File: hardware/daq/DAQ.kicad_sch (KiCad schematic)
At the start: 186 parts, among them J1 ICD15S13E4GX00LF, J2 ICD15S13E4GX00LF, J3 ICD15S13E4GX00LF, J4 ICD15S13E4GX00LF, P1 0022272021, U1 ADS124S08IRHBT, U11 SN74AHCT125RGYR, U2 ADS124S08IRHBT, U3 LT6654BMPS6-5-TRMPBF, U4 LM1086IS-5.0_NOPB, U5 TPS73801DCQR, U6 TPSM63603RDHR, U7 TPSM63603RDHR, U8 TPSM63603RDHR, U9 ADS124S08IRHBT

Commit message: routed 1.75 DSUBs
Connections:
- net FMV: now also D10.4; no longer D9.4
- net IDAC2_2: now also J1.12; no longer J1.11
- net PT10_SIG: now also J3.6; no longer J3.4
- net PT11_SIG: now also D3.4, J3.4; no longer D3.6, J3.6
- net PT12_SIG: now also D3.6, J3.14; no longer D3.4, J3.11
- net PT3_SIG: now also D9.4, J3.11; no longer D2.1, J3.14
- net PT7_SIG: now also D2.6; no longer D1.6
- net PT9_SIG: now also D1.6; no longer D2.6
- net RTD1_L1: now also J1.1; no longer J1.2
- net RTD1_L3: now also J1.2; no longer J1.1
- net RTD2_L1: now also J1.14; no longer J1.13
- net RTD2_L3: now also J1.13; no longer J1.12
- net RTD3_L3: now also J1.11; no longer J1.14

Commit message: 2 DSUBs???
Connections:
- net IDAC2_1: now also J2.14; no longer J1.3
- net PT4_SIG: now also J1.1; no longer J2.12
- net PT5_SIG: now also J1.2; no longer J2.13
- net PT6_SIG: now also J1.3; no longer J2.14
- net RTD1_L1: now also J2.12; no longer J1.1
- net RTD1_L3: now also J2.13; no longer J1.2
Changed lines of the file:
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@@
-		)
-	)
-	(label "PT4_SIG"
-		(at 347.98 346.71 0)
-		(fields_autoplaced yes)
-		(effects
-			(font
-				(size 1.27 1.27)
-			)
-			(justify left bottom)
-		)
-		(property "Netclass" ""
-			(at 347.98 347.98 0)
-			(effects
-				(font
-					(size 1.27 1.27)
-					(italic yes)
-				)
-				(justify left)
-			)
-		)
-	)
-	(label "PT6_SIG"
-		(at 347.98 351.79 0)
-		(fields_autoplaced yes)
-		(effects
-			(font
-				(size 1.27 1.27)
-			)
-			(justify left bottom)
-		)
-		(property "Netclass" ""
-			(at 347.98 353.06 0)
-			(effects
-				(font
-					(size 1.27 1.27)
-					(italic yes)
-				)
-				(justify left)
-			)
 		)
 	)
@@
 		)
 	)
+	(label "PT4_SIG"
+		(at 257.81 344.17 0)
+		(fields_autoplaced yes)
+		(effects
+			(font
+				(size 1.27 1.27)
+			)
+			(justify left bottom)
+		)
+		(property "Netclass" ""
+			(at 257.81 345.44 0)
+			(effects
+				(font
+					(size 1.27 1.27)
+					(italic yes)
+				)
+				(justify left)
+			)
+		)
+	)
 	(label "PT11_SIG"
 		(at 364.49 351.79 0)
@@
 		)
 	)
+	(label "PT5_SIG"
+		(at 257.81 346.71 0)
+		(fields_autoplaced yes)
+		(effects
+			(font
+				(size 1.27 1.27)
+			)
+			(justify left bottom)
+		)
+		(property "Netclass" ""
+			(at 257.81 347.98 0)
+			(effects
+				(font
+					(size 1.27 1.27)
+					(italic yes)
+				)
+				(justify left)
+			)
+		)
+	)
 	(label "LS1_SIG-"
 		(at 41.91 95.25 0)
@@
 		)
 	)
-	(label "RTD1_L1"
-		(at 257.81 344.17 0)
-		(effects
-			(font
-				(size 1.27 1.27)
-			)
-			(justify left bottom)
-		)
-	)
 	(label "IDAC2_1"
 		(at 53.34 76.2 0)
@@
 		)
 	)
+	(label "RTD1_L1"
+		(at 347.98 346.71 0)
+		(effects
+			(font
+				(size 1.27 1.27)
+			)
+			(justify left bottom)
+		)
+	)
 	(label "SCLK"
 		(at 218.44 91.44 0)
@@
 		)
 	)
+	(label "RTD1_L2"
+		(at 347.98 351.79 0)
+		(effects
+			(font
+				(size 1.27 1.27)
+			)
+			(justify left bottom)
+		)
+	)
 	(label "DATA_BUS"
 		(at 273.05 200.66 0)
@@
 		)
 	)
-	(label "PT5_SIG"
-		(at 347.98 349.25 0)
-		(fields_autoplaced yes)
-		(effects
-			(font
-				(size 1.27 1.27)
-			)
-			(justify left bottom)
-		)
-		(property "Netclass" ""
-			(at 347.98 350.52 0)
-			(effects
-				(font
-					(size 1.27 1.27)
-					(italic yes)
-				)
-				(justify left)
-			)
-		)
-	)
 	(label "FMV"
 		(at 443.23 54.61 0)
@@
 		)
 	)
+	(label "PT6_SIG"
+		(at 257.81 349.25 0)
+		(fields_autoplaced yes)
+		(effects
+			(font
+				(size 1.27 1.27)
+			)
+			(justify left bottom)
+		)
+		(property "Netclass" ""
+			(at 257.81 350.52 0)
+			(effects
+				(font
+					(size 1.27 1.27)
+					(italic yes)
+				)
+				(justify left)
+			)
+		)
+	)
 	(label "IDAC2_1"
 		(at 147.32 78.74 0)
@@
 		)
 	)
+	(label "RTD1_L3"
+		(at 347.98 349.25 0)
+		(effects
+			(font
+				(size 1.27 1.27)
+			)
+			(justify left bottom)
+		)
+	)
 	(label "LS2_SIG-"
 		(at 312.42 351.79 0)
@@
 		)
 	)
-	(label "RTD1_L3"
-		(at 257.81 346.71 0)
-		(effects
-			(font
-				(size 1.27 1.27)
-			)
-			(justify left bottom)
-		)
-	)
 	(label "OIMV{slash}FIMV{slash}SPARK"
 		(at 537.21 64.77 0)
@@
 		(effects
 			(font
-				(size 1.27 1.27)
-			)
-			(justify left bottom)
-		)
-	)
-	(label "RTD1_L2"
-		(at 257.81 349.25 0)
-		(effects
-			(font

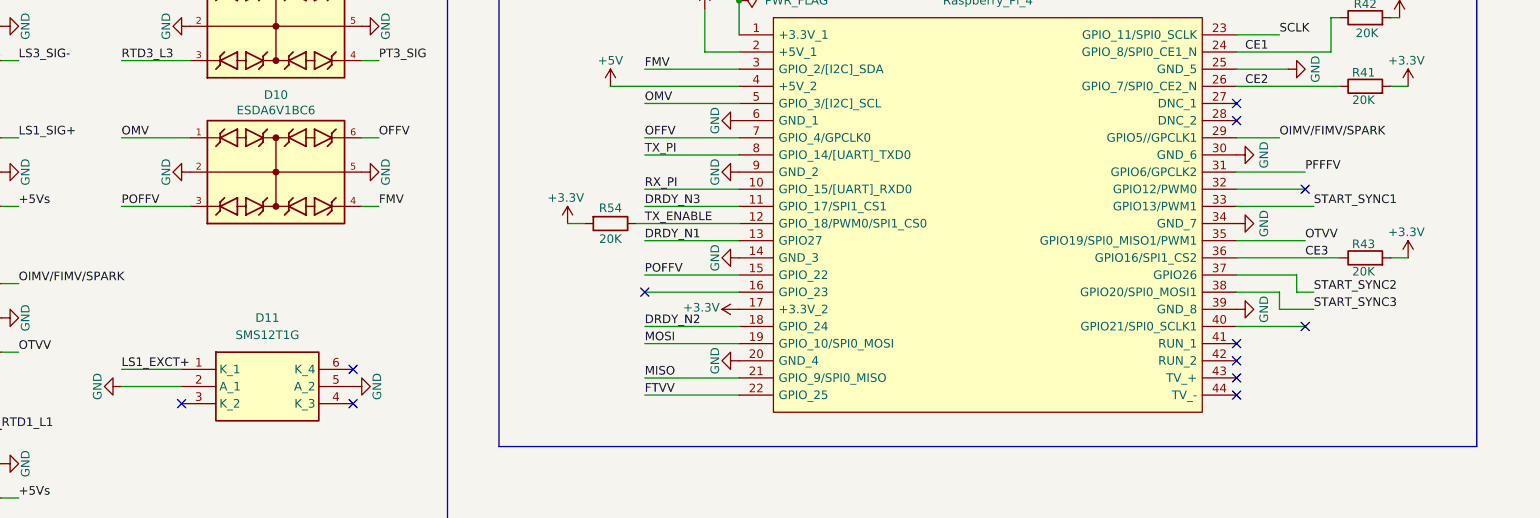
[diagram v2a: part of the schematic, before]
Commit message: routed valve actuation traces thu TVS and GPIO
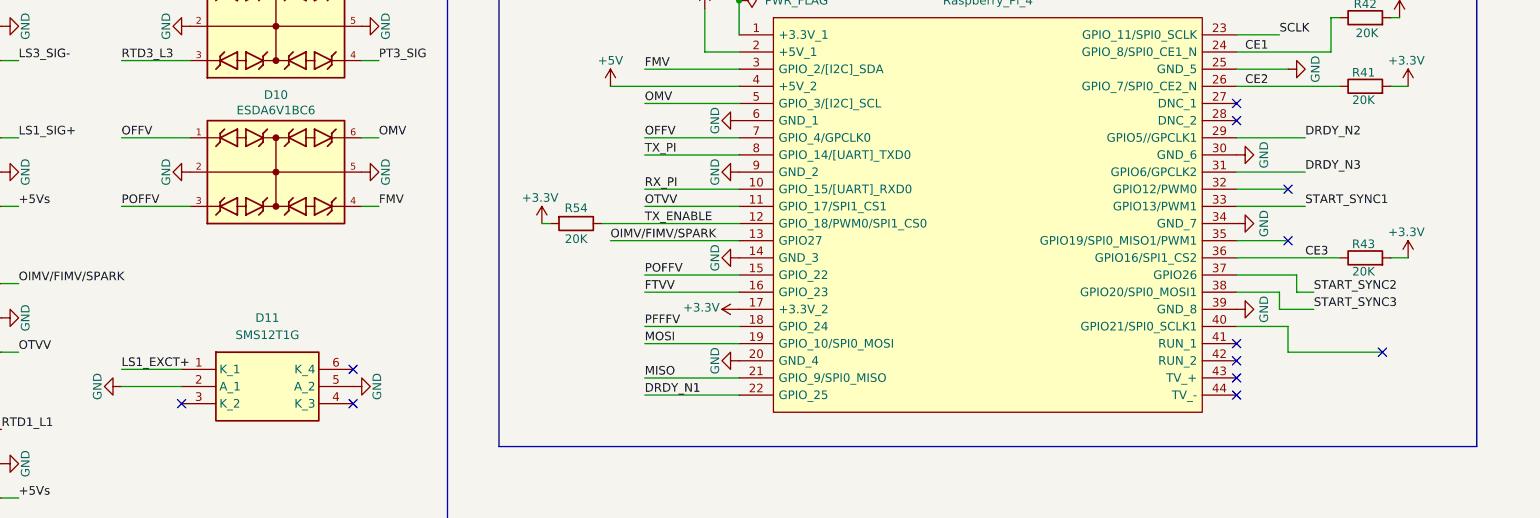
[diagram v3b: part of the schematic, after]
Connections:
- net DRDY_N1: now also RP1.22 (GPIO_25); no longer RP1.13 (GPIO27)
- net DRDY_N2: now also RP1.29 (GPIO5//GPCLK1); no longer RP1.18 (GPIO_24)
- net DRDY_N3: now also RP1.31 (GPIO6/GPCLK2); no longer RP1.11 (GPIO_17/SPI1_CS1)
- net FTVV: now also RP1.16 (GPIO_23); no longer RP1.22 (GPIO_25)
- net OFFV: now also D10.1; no longer D10.6
- net OIMV/FIMV/SPARK: now also RP1.13 (GPIO27); no longer RP1.29 (GPIO5//GPCLK1)
- net OMV: now also D10.6; no longer D10.1
- net OTVV: now also RP1.11 (GPIO_17/SPI1_CS1); no longer RP1.35 (GPIO19/SPI0_MISO1/PWM1)
- net PFFFV: now also RP1.18 (GPIO_24); no longer RP1.31 (GPIO6/GPCLK2)
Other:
- moved on the sheet: R54

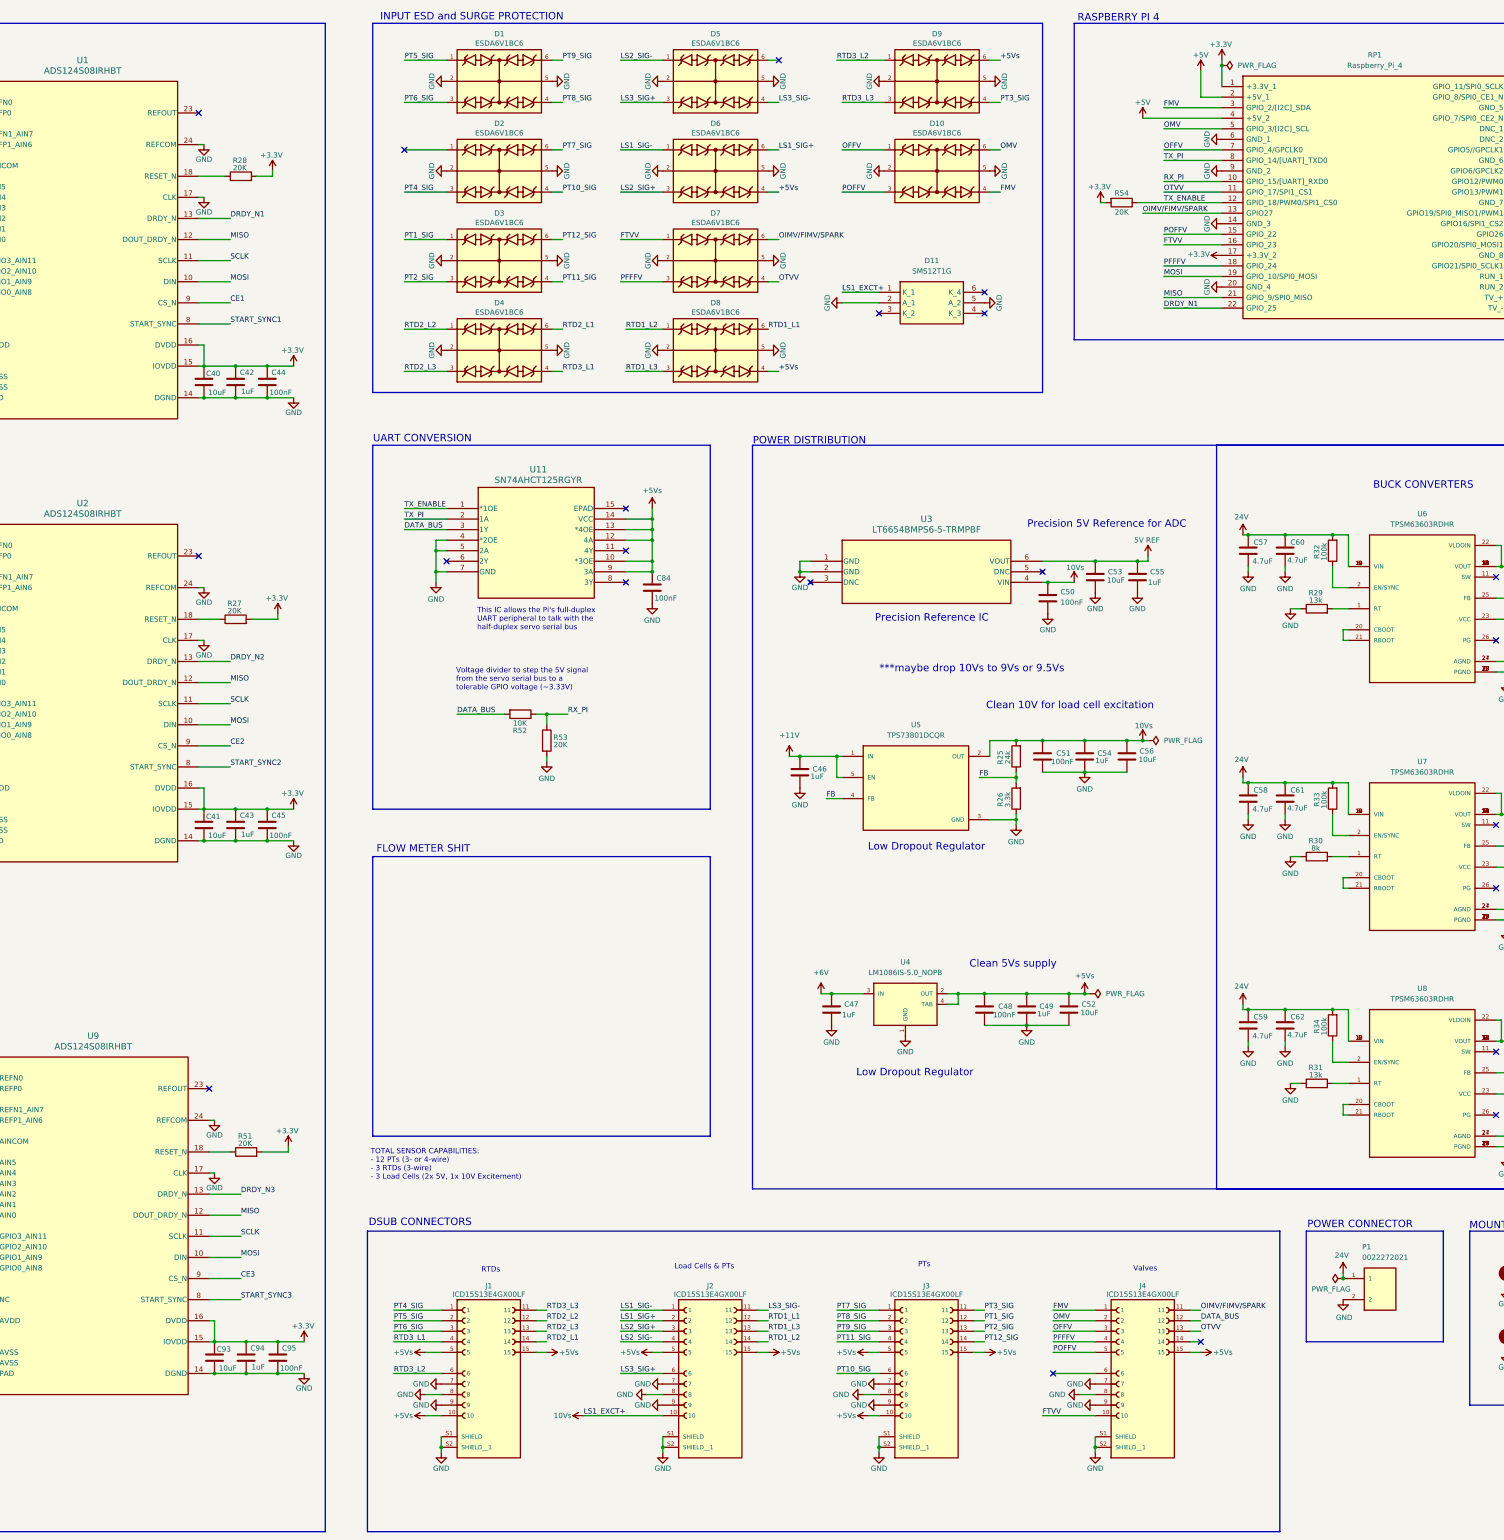
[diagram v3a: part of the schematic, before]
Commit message: reordered references and started power traces
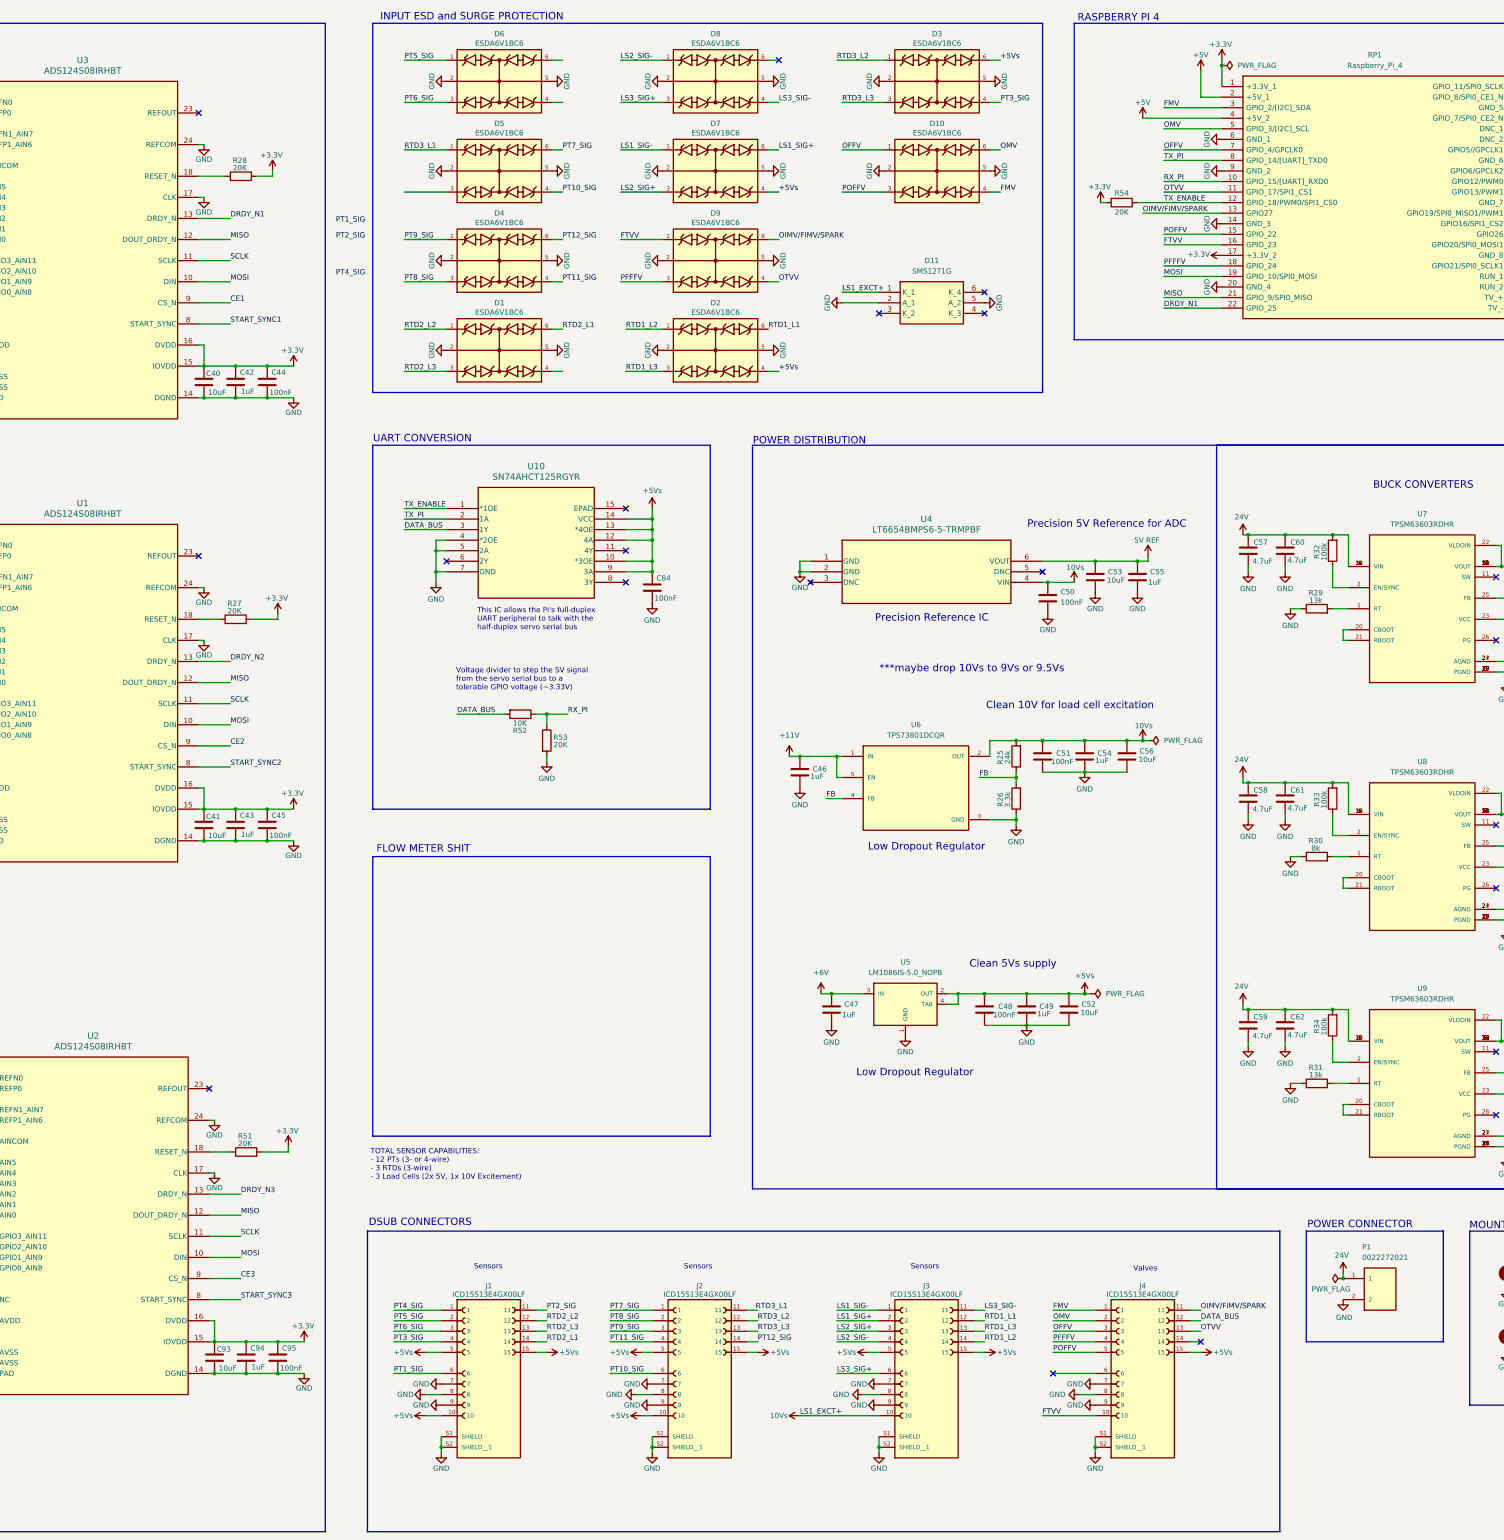
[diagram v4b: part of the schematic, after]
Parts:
- renumbered D4 to D1, D8 to D2, D9 to D3, D3 to D4, D2 to D5, D1 to D6, D6 to D7, D5 to D8, D7 to D9, J3 to J2, J2 to J3, U2 to U1, U11 to U10, U9 to U2, U1 to U3, U3 to U4, U4 to U5, U5 to U6, U6 to U7, U7 to U8, U8 to U9
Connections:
- net IDAC2_3: now also J2.12; no longer J1.6
- net PT1_SIG: now also J1.6; no longer D4.1, J2.12
- net PT2_SIG: now also J1.11; no longer D4.3, J2.13
- net PT3_SIG: now also J1.4; no longer J2.11
- net PT4_SIG: no longer D5.3
- net PT8_SIG: now also D4.3; no longer D6.4
- net PT9_SIG: now also D4.1; no longer D6.6
- net RTD3_L1: now also D5.1, J2.11; no longer D1.4, J1.4
- net RTD3_L3: now also J2.13; no longer J1.11
- no-connect marks 34 -> 33
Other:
- note added: "Sensors"
- note removed: "Load Cells & PTs"
- note removed: "PTs"
- note removed: "RTDs"
- moved on the sheet: J2, J3
